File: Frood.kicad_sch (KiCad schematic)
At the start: 40 parts, among them J1 Left, J2 Right, J3 Bottom, SW1 RESET, SW2 BOOT, U1 RP2040, U2 W25Q32JWUUIQ, U3 SPX3819M5-L-3-3/TR, Y1 X322512MSB4SI

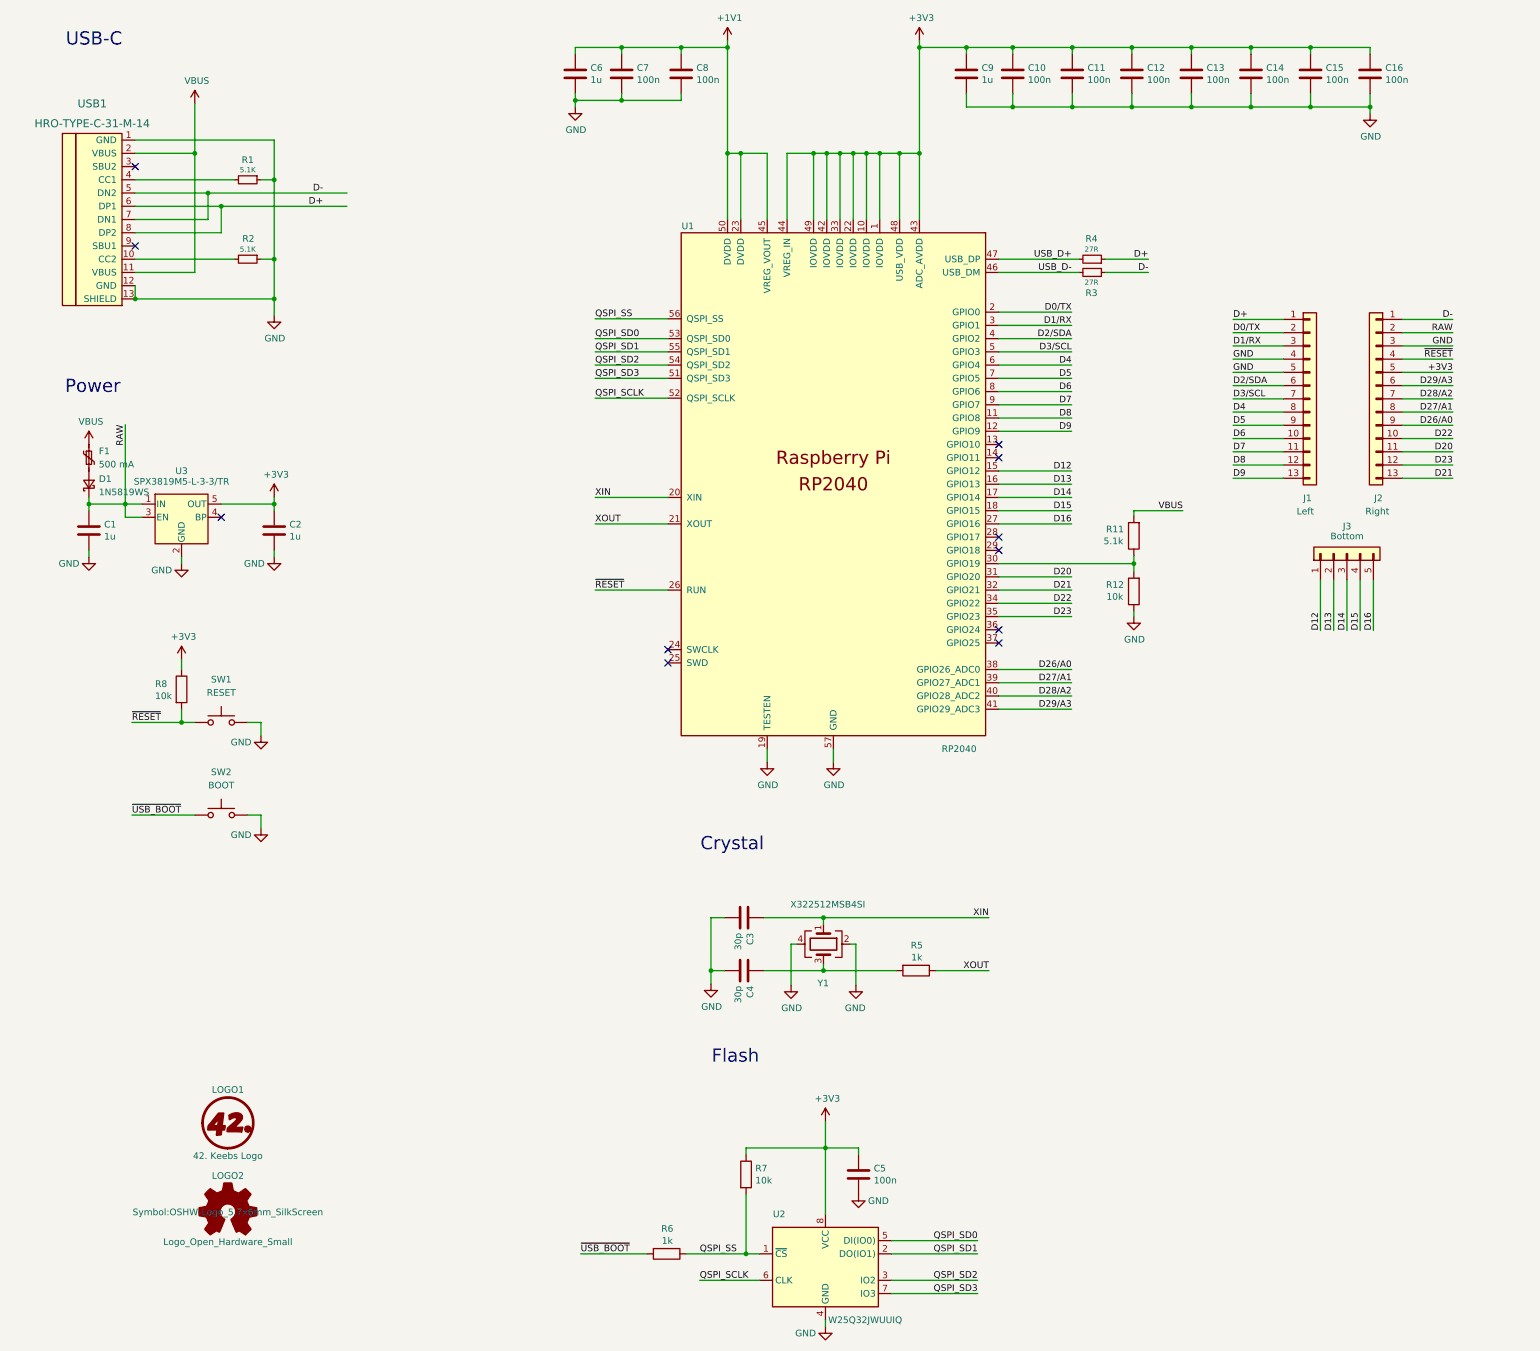
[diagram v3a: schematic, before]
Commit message: Rev4 update
* Use correctly-specced 16 Mbit QSPI flash
* Switch to fully mid-mounted GT-USB-7014C USB-C socket and 1.6 mm PCB
* Improve pin labels
* Improve routing
* Update the README with version history
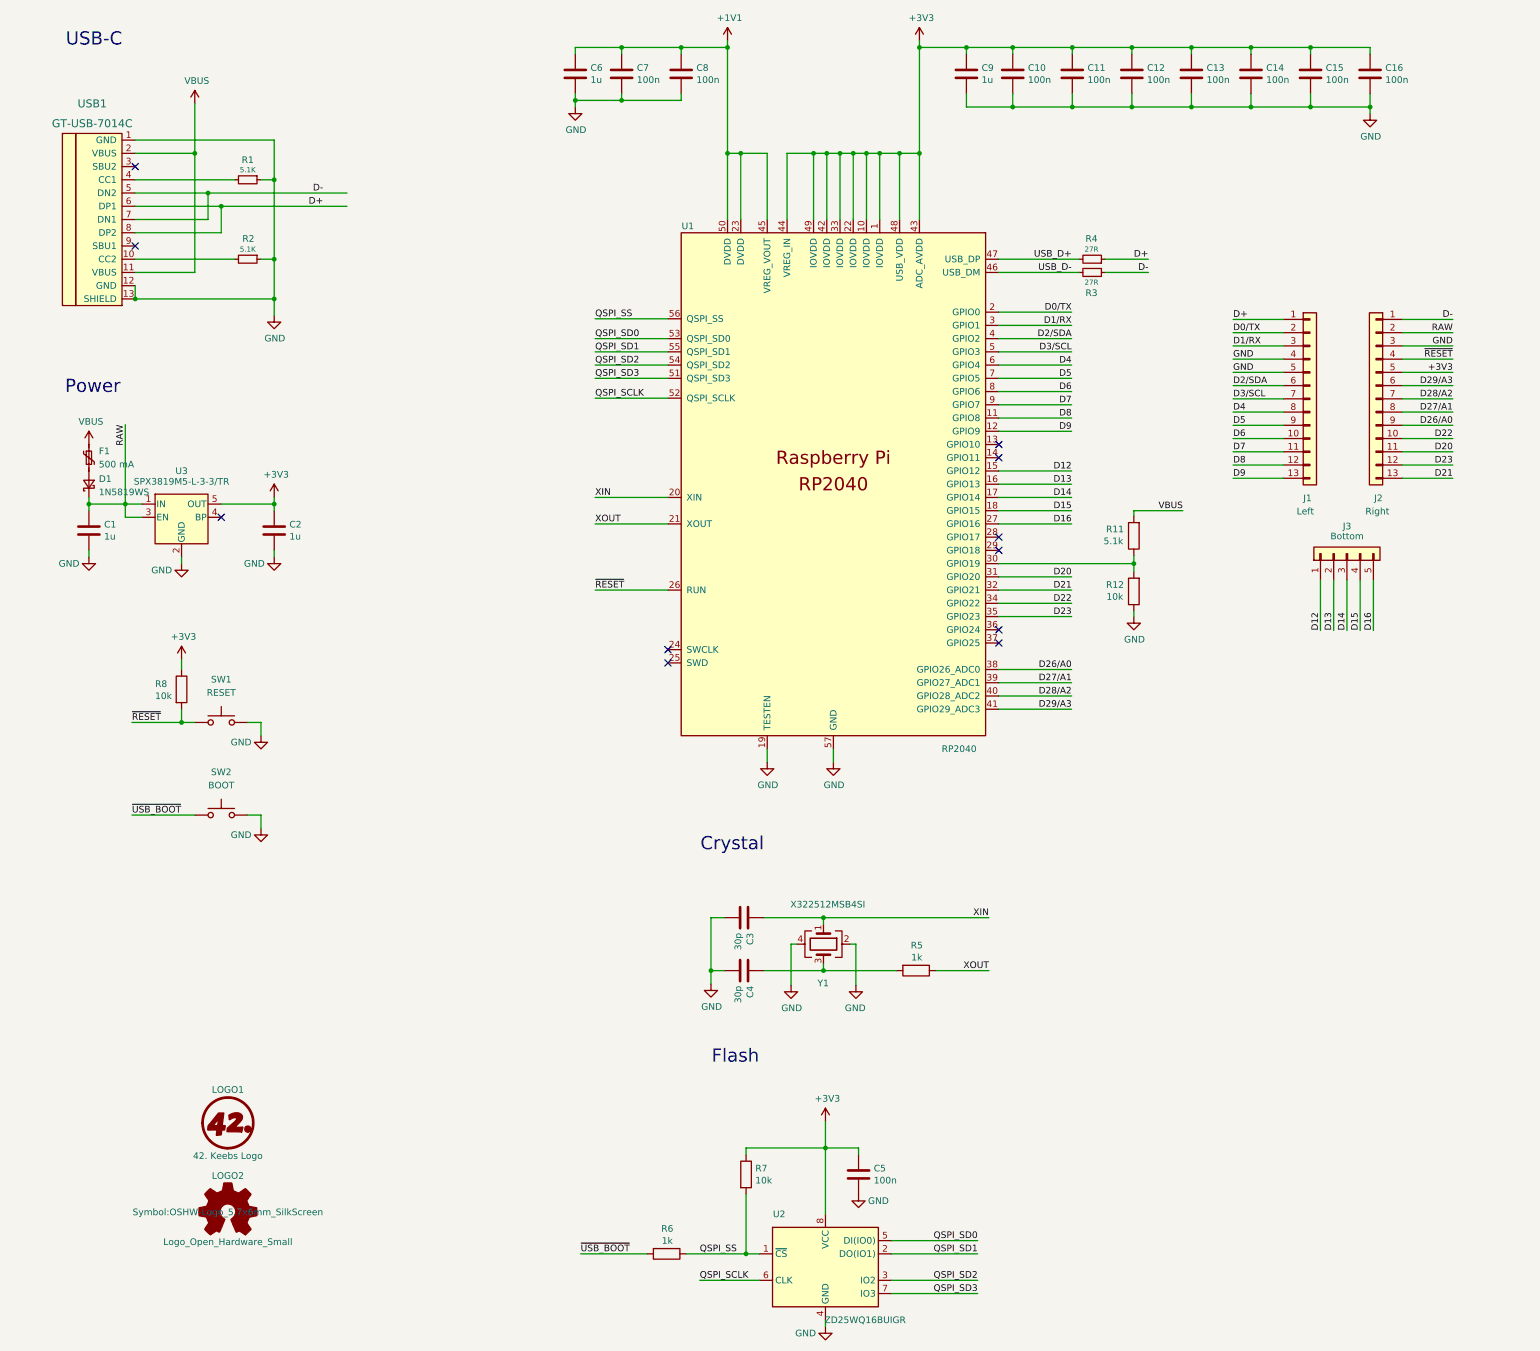
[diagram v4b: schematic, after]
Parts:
- U2: value W25Q32JWUUIQ -> ZD25WQ16BUIGR; footprint 42keebs:USON-8_4x3mm_P0.8mm -> 42keebs:DFN-8-1EP_3x2mm_P0.5mm_EP0.2x1.6mm; LCSC C2760370 -> C2759920
- USB1: value HRO-TYPE-C-31-M-14 -> GT-USB-7014C; footprint 42keebs:TYPE-C-31-M-14-PiMicro -> 42keebs:Molex-216990_GCT-USB45xx_HRO-TYPE-C-31-M-13x-PiMicro
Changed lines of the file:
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@@
       (effects (font (size 1.524 1.524)))
     )
-    (property "Value" "HRO-TYPE-C-31-M-14" (id 1) (at 29.21 35.56 0)
+    (property "Value" "GT-USB-7014C" (id 1) (at 29.21 35.56 0)
       (effects (font (size 1.524 1.524)))
     )
-    (property "Footprint" "42keebs:TYPE-C-31-M-14-PiMicro" (id 2) (at 34.925 52.705 0)
+    (property "Footprint" "42keebs:Molex-216990_GCT-USB45xx_HRO-TYPE-C-31-M-13x-PiMicro" (id 2) (at 34.925 52.705 0)
       (effects (font (size 1.524 1.524)) hide)
     )
@@
     (in_bom yes) (on_board yes)
     (property "Reference" "U2" (id 0) (at 161.036 244.856 0))
-    (property "Value" "W25Q32JWUUIQ" (id 1) (at 177.546 265.176 0))
-    (property "Footprint" "42keebs:USON-8_4x3mm_P0.8mm" (id 2) (at 169.926 255.016 0)
+    (property "Value" "ZD25WQ16BUIGR" (id 1) (at 177.546 265.176 0))
+    (property "Footprint" "42keebs:DFN-8-1EP_3x2mm_P0.5mm_EP0.2x1.6mm" (id 2) (at 169.926 255.016 0)
       (effects (font (size 1.27 1.27)) hide)
     )
@@
       (effects (font (size 1.27 1.27)) hide)
     )
-    (property "LCSC" "C2760370" (id 4) (at 169.926 255.016 0)
+    (property "LCSC" "C2759920" (id 4) (at 169.926 255.016 0)
       (effects (font (size 1.27 1.27)) hide)
     )
@@
     )
     (path "/80130354-2922-4669-916a-ca379b7dd9a6"
-      (reference "U2") (unit 1) (value "W25Q32JWUUIQ") (footprint "42keebs:USON-8_4x3mm_P0.8mm")
+      (reference "U2") (unit 1) (value "ZD25WQ16BUIGR") (footprint "42keebs:DFN-8-1EP_3x2mm_P0.5mm_EP0.2x1.6mm")
     )
     (path "/c779cfe3-909f-43ee-bfb4-4bb9da9ab75d"
@@
     )
     (path "/22bd63ac-0dc8-46a4-b634-819479c04be4"
-      (reference "USB1") (unit 1) (value "HRO-TYPE-C-31-M-14") (footprint "42keebs:TYPE-C-31-M-14-PiMicro")
+      (reference "USB1") (unit 1) (value "GT-USB-7014C") (footprint "42keebs:Molex-216990_GCT-USB45xx_HRO-TYPE-C-31-M-13x-PiMicro")
     )
     (path "/dec5c5bc-8eeb-4827-91ed-4f4f63dc849a"

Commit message: Improve USB socket position; add boot/reset pads on the bottom
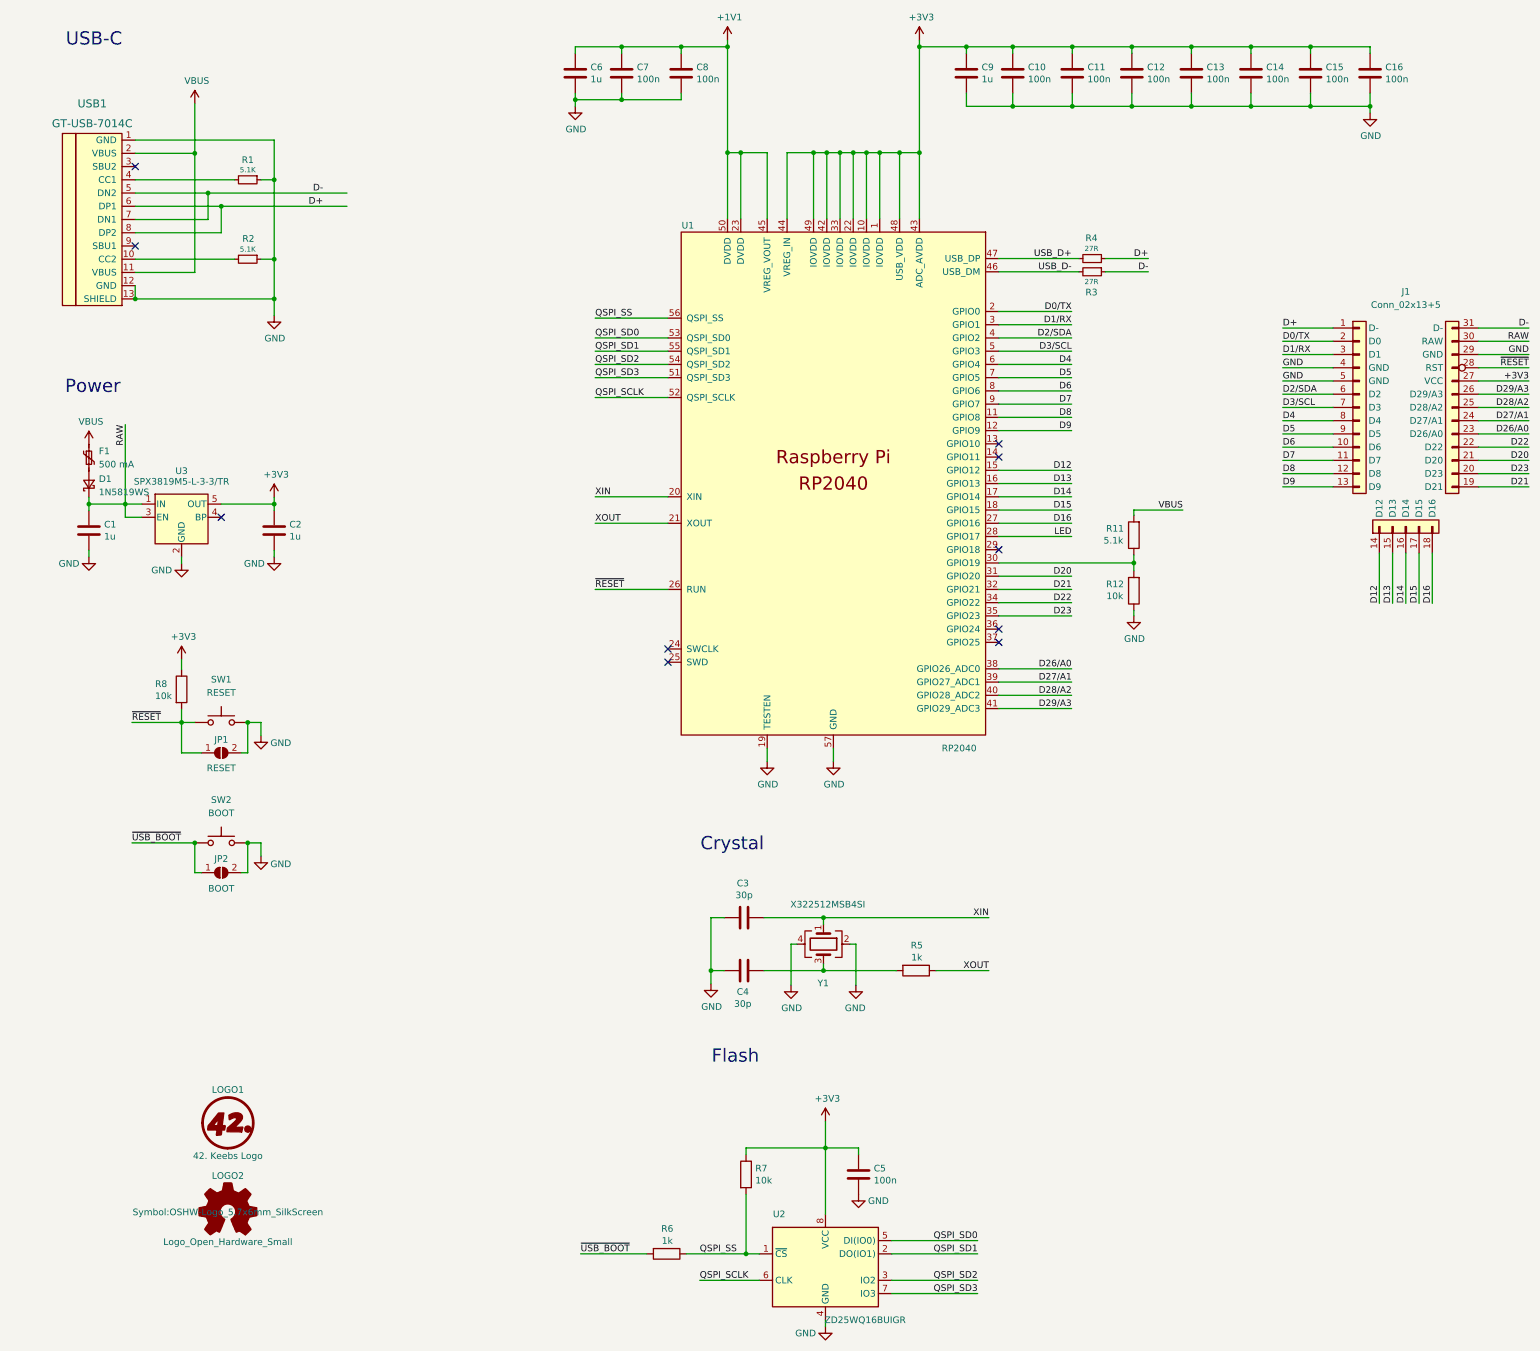
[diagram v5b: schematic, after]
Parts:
- removed J1: Left, 42keebs:PinHeader_1x13_P2.54mm_Vertical_ProMicro-Left, symbol Connector_Generic:Conn_01x13
- removed J2: Right, 42keebs:PinHeader_1x13_P2.54mm_Vertical_ProMicro-Right, symbol Connector_Generic:Conn_01x13
- removed J3: Bottom, 42keebs:PinHeader_1x05_P2.54mm_Vertical_Plain, symbol Connector_Generic:Conn_01x05
- added J1: Conn_02x13+5, 42keebs:PinHeader_2x13+5_P2.54mm_Vertical_Elite-C, symbol 42keebs:Conn_02x13+5
- added JP1: RESET, Jumper:SolderJumper-2_P1.3mm_Open_RoundedPad1.0x1.5mm, symbol Jumper:SolderJumper_2_Open
- added JP2: BOOT, Jumper:SolderJumper-2_P1.3mm_Open_RoundedPad1.0x1.5mm, symbol Jumper:SolderJumper_2_Open
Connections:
- net +3V3: now also J1.27 (VCC)
- net D+: now also J1.1 (D-)
- net D-: now also J1.31 (D-)
- net D0/TX: now also J1.2 (D0)
- net D12: now also J1.14 (D12)
- net D13: now also J1.15 (D13)
- net D14: now also J1.16 (D14)
- net D15: now also J1.17 (D15)
- net D16: now also J1.18 (D16)
- net D1/RX: now also J1.3 (D1)
- net D20: now also J1.21 (D20)
- net D21: now also J1.19 (D21)
- net D22: now also J1.22 (D22)
- net D23: now also J1.20 (D23)
- net D26/A0: now also J1.23 (D26/A0)
- net D27/A1: now also J1.24 (D27/A1)
- net D28/A2: now also J1.25 (D28/A2)
- net D29/A3: now also J1.26 (D29/A3)
- net D2/SDA: now also J1.6 (D2)
- net D3/SCL: now also J1.7 (D3)
- net D4: now also J1.8 (D4)
- net D5: now also J1.9 (D5)
- net D6: now also J1.10 (D6)
- net D7: now also J1.11 (D7)
- net D8: now also J1.12 (D8)
- net D9: now also J1.13 (D9)
- net GND: now also J1.29 (GND), J1.4 (GND), J1.5 (GND), JP1.2 (B), JP2.2 (B)
- net RAW: now also J1.30 (RAW)
- net ~{RESET}: now also J1.28 (RST), JP1.1 (A)
- net ~{USB_BOOT}: now also JP2.1 (A)
- net LED: now reaches U1.28 (GPIO17)
- no-connect marks 11 -> 10
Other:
- moved on the sheet: SW2

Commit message: Rev5 update
* Use a smaller crystal to get some valuable space back
* Add an orange indicator LED on pin GPIO17
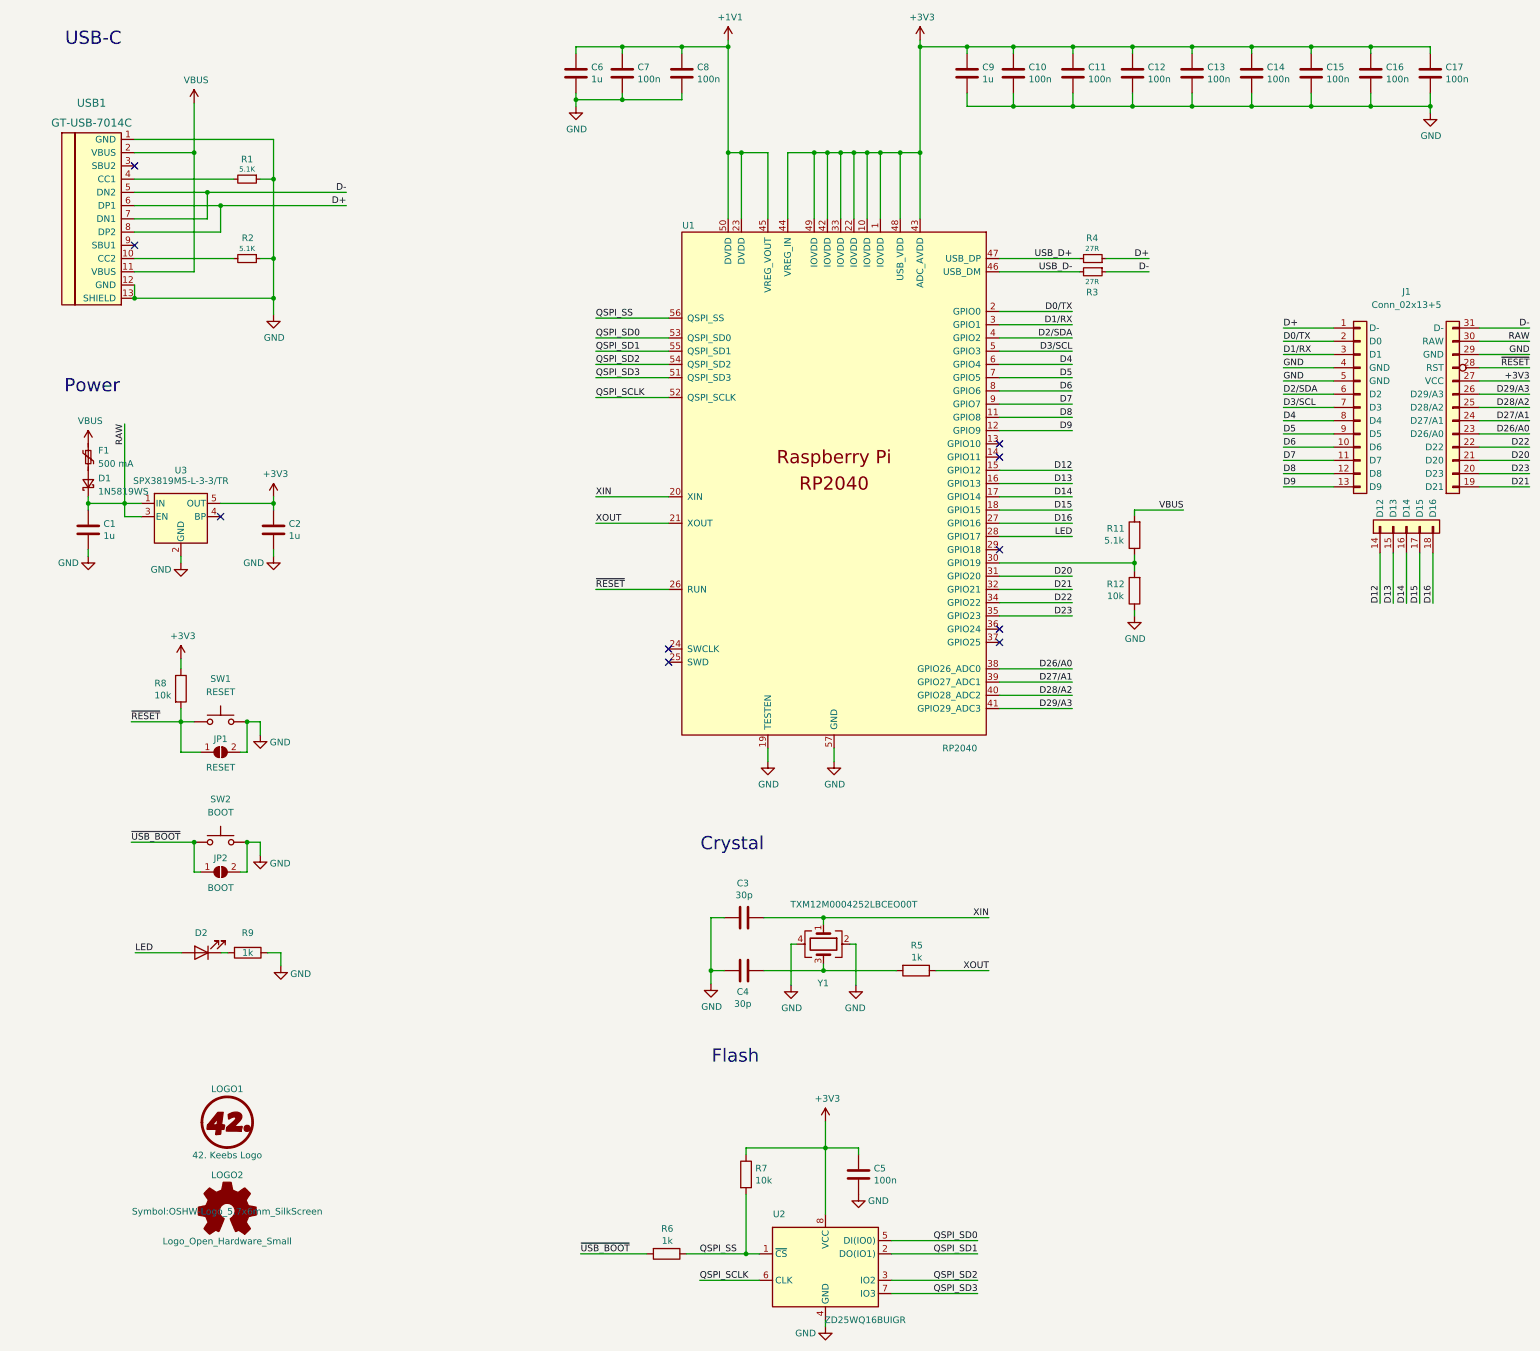
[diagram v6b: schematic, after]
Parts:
- added C17: 100n, Capacitor_SMD:C_0402_1005Metric, symbol Device:C
- added D2: LED, LED_SMD:LED_0402_1005Metric, symbol Device:LED
- added R9: 1k, Resistor_SMD:R_0402_1005Metric, symbol Device:R
- Y1: value X322512MSB4SI -> TXM12M0004252LBCEO00T; footprint Crystal:Crystal_SMD_3225-4Pin_3.2x2.5mm -> Crystal:Crystal_SMD_2520-4Pin_2.5x2.0mm; PartNo C9002 -> C284156
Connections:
- net +3V3: now also C17.1
- net GND: now also C17.2, R9.1
- net LED: now also D2.2 (A)
- new net: D2.1 (K), R9.2
